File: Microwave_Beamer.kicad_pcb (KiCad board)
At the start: 6 copper layers, 200 x 170 mm, 408 parts, among them IC1 MAX2870ETJ+, U1 SKY13575-639LF, U10 SKY13575-639LF, U11 SKY13575-639LF, U12 SKY13575-639LF, U13 SE5023L-R, U14 SE5023L-R, U15 SE5023L-R, U16 SE5023L-R, U17 SE5023L-R, U18 SE5023L-R, U19 SE5023L-R, U2 SKY13575-639LF, U20 SE5023L-R, U21 SE5023L-R, U22 SE5023L-R, U23 SE5023L-R, U24 SE5023L-R, U25 SE5023L-R, U26 SE5023L-R, U27 SE5023L-R, U28 SE5023L-R, U29 SE5023L-R, U3 SKY13575-639LF, U30 SE5023L-R, U31 SE5023L-R, U32 SE5023L-R, U33 SE5023L-R, U34 SE5023L-R, U35 SE5023L-R, U36 SE5023L-R, U37 SE5023L-R, U38 SE5023L-R, U39 SE5023L-R, U4 SKY13575-639LF, U40 SE5023L-R, U41 SE5023L-R, U42 SE5023L-R, U43 SE5023L-R, U44 SE5023L-R, U45 SE5023L-R, U46 SE5023L-R, U47 SE5023L-R, U48 SE5023L-R, U49 SE5023L-R, U5 SKY13575-639LF, U50 LDL1117S33R, U51 SN74LVC1G14DCKR, U52 MIC5219-2.85YM5-TR, U53 SN74LVC1G14DCKR, U54 74HC138D, U55 TPS548D26RXXR, U56 PI_PICO, U57 SN74LVC1G14DCKR, U6 SKY13575-639LF, U7 SKY13575-639LF, U8 SKY13575-639LF, U9 SKY13575-639LF, Y1 ECS-3225MVQ-1000-CN-TR

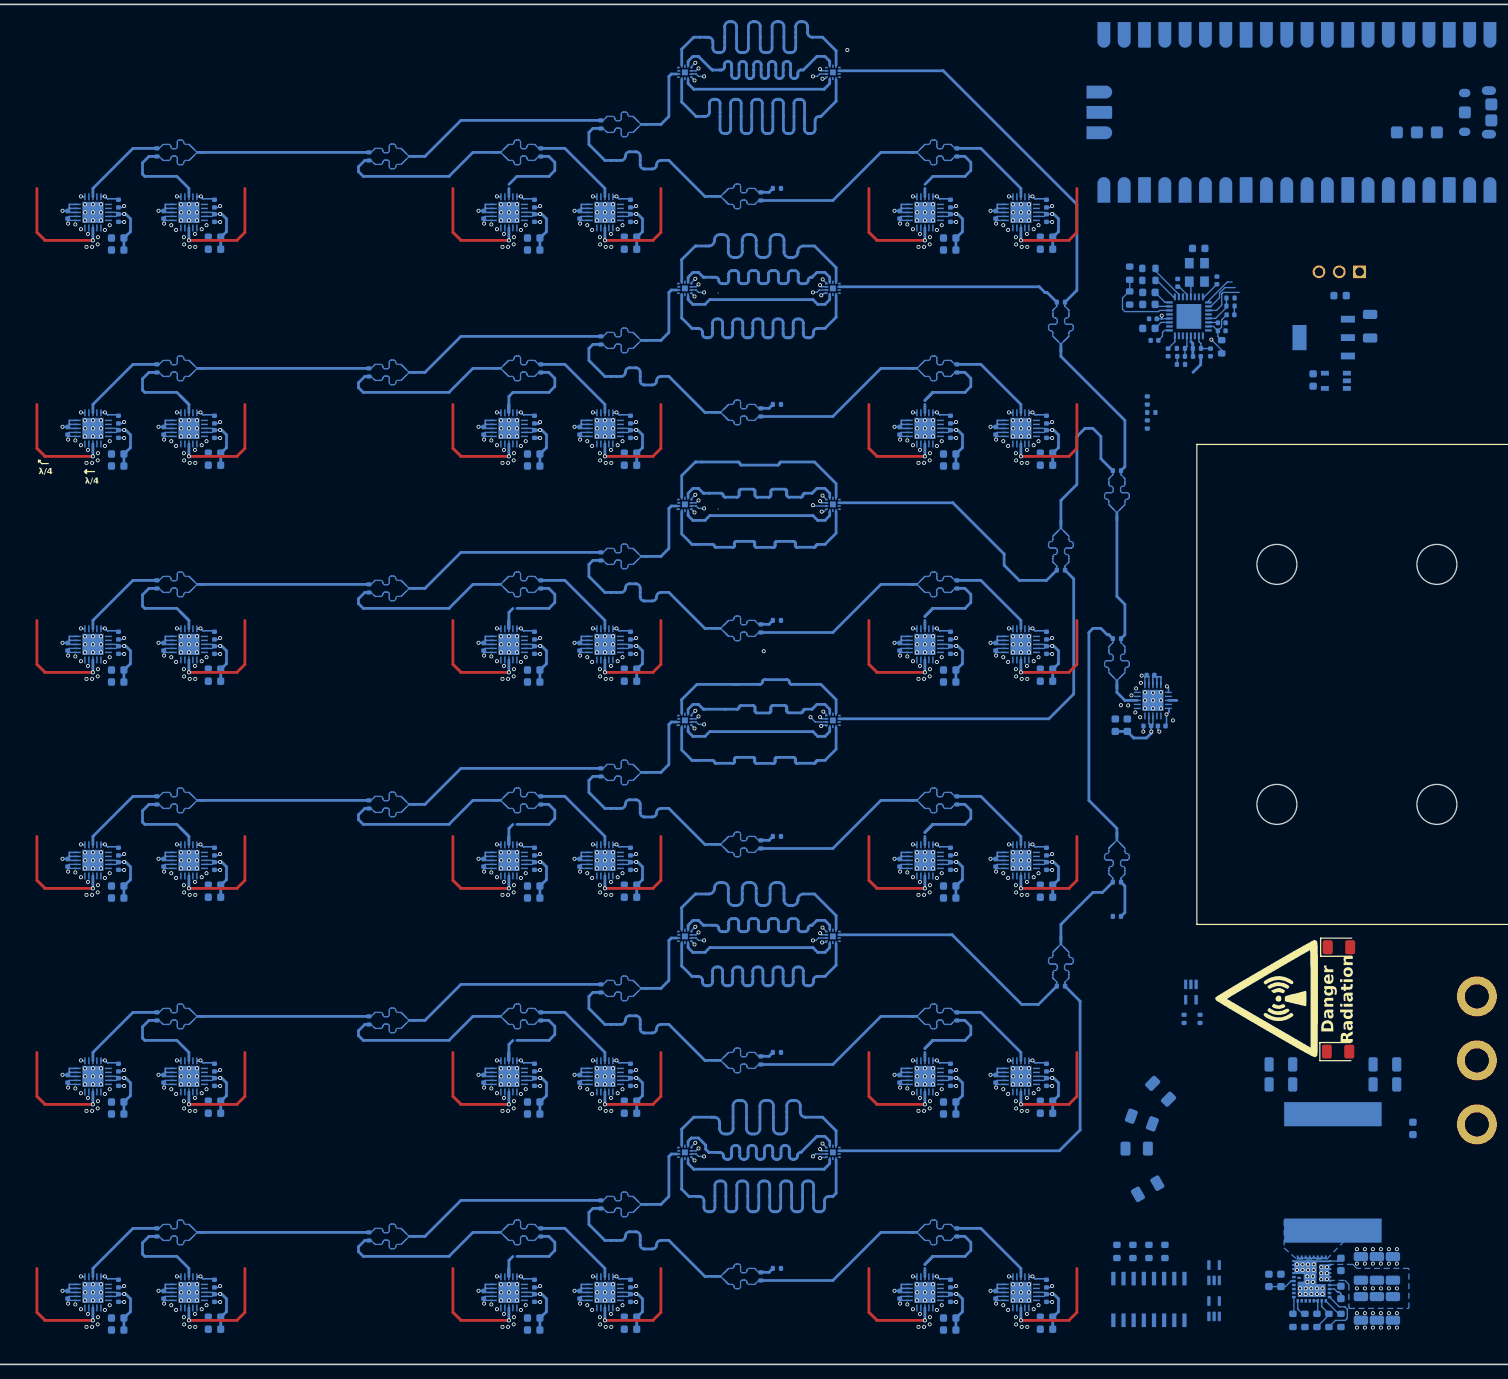
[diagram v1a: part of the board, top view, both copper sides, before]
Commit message: completed length matching
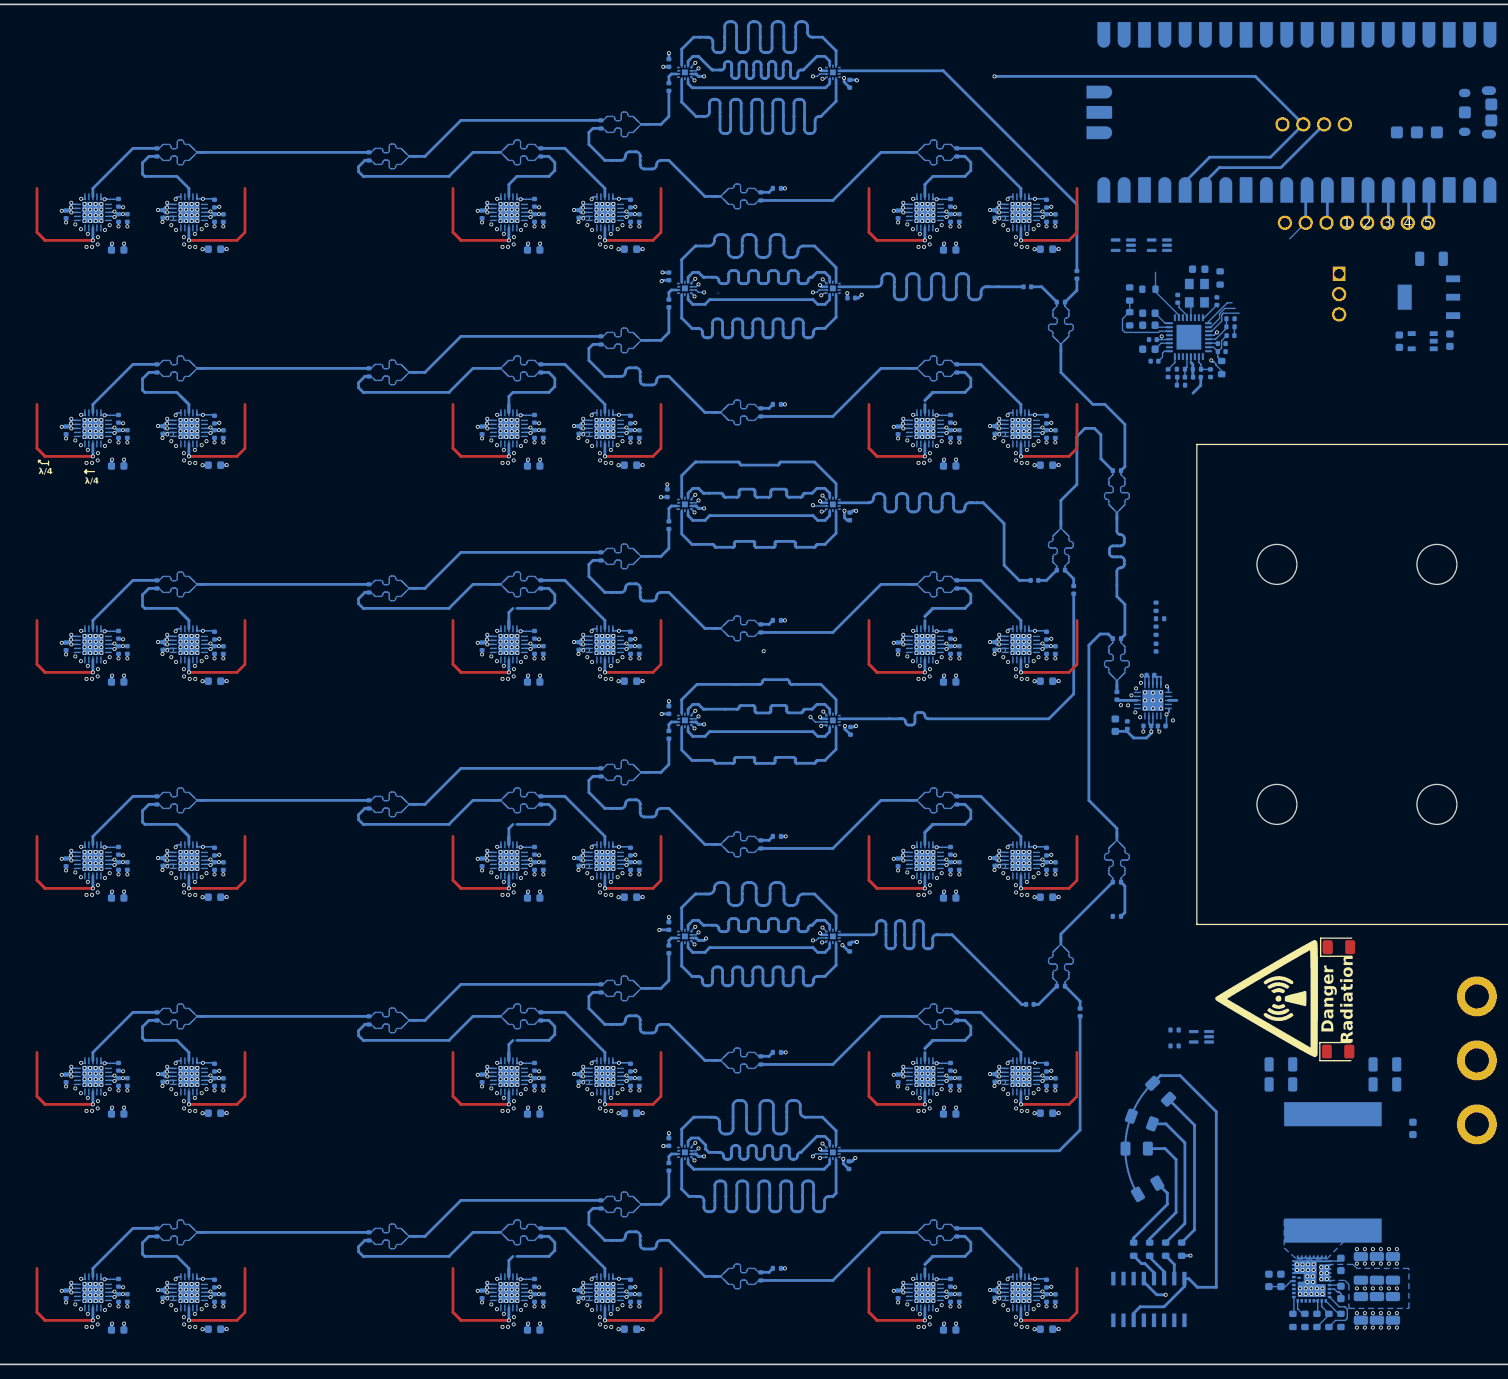
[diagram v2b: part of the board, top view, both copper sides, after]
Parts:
- added 1: , , F.Cu at (188.7, 32.3)
- added 2: , , F.Cu at (191.3, 32.3)
- added 3: , , F.Cu at (193.8, 32.3)
- added 4: , , F.Cu at (196.4, 32.3)
- added 5: , , F.Cu at (198.9, 32.3)
- added ?: , , F.Cu at (185.9, 20.0)
- added ?: , , F.Cu at (188.5, 20.0)
- added ?: , , F.Cu at (183.3, 20.0)
- added ?: , , F.Cu at (186.2, 32.3)
- added ?: , , F.Cu at (183.6, 32.3)
- added ?: , , F.Cu at (180.7, 20.0)
- added ?: , , F.Cu at (181.0, 32.3)
- added C139: 2.2pF, Capacitor_SMD:C_0402_1005Metric, B.Cu at (160.0, 91.4)
- added C140: 10nF, Capacitor_SMD:C_0402_1005Metric, B.Cu at (126.6, 14.9)
- added C147: 10nF, Capacitor_SMD:C_0402_1005Metric, B.Cu at (126.8, 41.7)
- added C148: 10nF, Capacitor_SMD:C_0402_1005Metric, B.Cu at (103.8, 66.1)
- added C149: 10nF, Capacitor_SMD:C_0402_1005Metric, B.Cu at (104.0, 93.2)
- added C151: 10nF, Capacitor_SMD:C_0402_1005Metric, B.Cu at (104.0, 120.2)
- added C152: 10nF, Capacitor_SMD:C_0402_1005Metric, B.Cu at (126.5, 150.1)
- added C153: 10nF, Capacitor_SMD:C_0402_1005Metric, B.Cu at (104.0, 12.3)
- added C154: 10nF, Capacitor_SMD:C_0402_1005Metric, B.Cu at (104.0, 147.2)
- added C155: 10nF, Capacitor_SMD:C_0402_1005Metric, B.Cu at (104.0, 39.0)
- added C156: 10nF, Capacitor_SMD:C_0402_1005Metric, B.Cu at (126.6, 69.0)
- added C158: 10nF, Capacitor_SMD:C_0402_1005Metric, B.Cu at (126.7, 95.8)
- added C160: 10nF, Capacitor_SMD:C_0402_1005Metric, B.Cu at (126.6, 122.9)
- added C161: 2.2pF, Capacitor_SMD:C_0402_1005Metric, B.Cu at (104.0, 15.3)
- added C162: 2.2pF, Capacitor_SMD:C_0402_1005Metric, B.Cu at (104.0, 42.4)
- added C163: 2.2pF, Capacitor_SMD:C_0402_1005Metric, B.Cu at (104.0, 70.1)
- added C165: 2.2pF, Capacitor_SMD:C_0402_1005Metric, B.Cu at (104.0, 96.3)
- added C166: 2.2pF, Capacitor_SMD:C_0402_1005Metric, B.Cu at (104.0, 123.1)
- added C167: 2.2pF, Capacitor_SMD:C_0402_1005Metric, B.Cu at (104.0, 150.3)
- added C168: 2.2pF, Capacitor_SMD:C_0402_1005Metric, B.Cu at (155.0, 38.8)
- added C169: 2.2pF, Capacitor_SMD:C_0402_1005Metric, B.Cu at (148.8, 40.3)
- added C170: 2.2pF, Capacitor_SMD:C_0402_1005Metric, B.Cu at (149.7, 77.0)
- added C172: 2.2pF, Capacitor_SMD:C_0402_1005Metric, B.Cu at (154.6, 78.2)
- added C174: 2.2pF, Capacitor_SMD:C_0402_1005Metric, B.Cu at (149.1, 130.0)
- added C175: 2.2pF, Capacitor_SMD:C_0402_1005Metric, B.Cu at (155.4, 131.0)
- added C176: 2.2pF, Capacitor_SMD:C_0402_1005Metric, B.Cu at (164.9, 85.4)
- C107, C111, C114, C119, C12, C14, C16, C19, C21, C23, C25, C27, C28, C29, C30, C33, C35, C37, C39, C4, C41, C42, C43, C44, C46, C48, C49, C50, C6, C7, C71, C8, C82, C85, C9, C96, C99: footprint Capacitor_SMD:C_0603_1608Metric -> Capacitor_SMD:C_0402_1005Metric
- C285, C286, C287, C288, C289, C290, C291, C292, C293, C294, C295, C296, C297, C298, C299, C300, C301, C302, C303, C304, C305, C306, C307, C308, C309, C310, C311, C312, C313, C314, C315, C316, C317, C318, C319, C320, C321: value 10nF -> 100nF
- moved U53 133.1 mm to (165.3, 35.1), turned to 180 degrees
- moved U51 128.9 mm to (160.8, 35.1), turned to 180 degrees
- moved RR4 25.8 mm to (164.9, 80.3)
- moved RR5 25.8 mm to (165.4, 81.8)
- moved RR6 25.8 mm to (164.9, 83.3)
- moved C283 14.8 mm to (201.6, 47.0), turned to -90 degrees
- moved U50 14.1 mm to (199.0, 41.6)
- moved U52 11.9 mm to (198.2, 47.1)
- moved C284 11.8 mm to (195.3, 47.1)
- moved CB13 11.4 mm to (199.3, 36.8), turned to 0 degrees
- moved R54 8.91 mm to (172.9, 39.2), turned to 90 degrees
- moved U57 5.74 mm to (170.6, 134.1), turned to 180 degrees
- moved PS1 4.90 mm to (186.0, 41.2), turned to -90 degrees
- moved R61 4.64 mm to (167.2, 135.2), turned to 180 degrees
- moved C7 2.77 mm to (140.3, 31.7), turned to -90 degrees
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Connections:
- R4 pad 1: Net-(U1-RFC) -> Net-(W4-Out1)
- R4 pad 2: Net-(U2-RFC) -> Net-(W4-Out2)
- R5 pad 1: Net-(U3-RFC) -> Net-(W5-Out1)
- R5 pad 2: Net-(U4-RFC) -> Net-(W5-Out2)
- R6 pad 1: Net-(U5-RFC) -> Net-(W6-Out1)
- R6 pad 2: Net-(U6-RFC) -> Net-(W6-Out2)
- RR6 pad 2: /POWER AMP6/RF_IN -> Net-(C176-Pad1)
- U10 pad 2: /STEM/FAN_D/IN -> Net-(U10-RFC)
- U11 pad 2: /STEM/FAN_E/IN -> Net-(U11-RFC)
- U12 pad 2: /STEM/FAN_F/IN -> Net-(U12-RFC)
- U7 pad 2: /STEM/FAN_A/IN -> Net-(U7-RFC)
- U8 pad 2: /STEM/FAN_B/IN -> Net-(U8-RFC)
- U9 pad 2: /STEM/FAN_C/IN -> Net-(U9-RFC)
- W1 pad 1: /POWER AMP6/RF_OUT -> /STEM/IN
- W4 pad 2: Net-(U1-RFC) -> Net-(W4-Out1)
- W4 pad 3: Net-(U2-RFC) -> Net-(W4-Out2)
- W5 pad 2: Net-(U3-RFC) -> Net-(W5-Out1)
- W5 pad 3: Net-(U4-RFC) -> Net-(W5-Out2)
- W6 pad 2: Net-(U5-RFC) -> Net-(W6-Out1)
- W6 pad 3: Net-(U6-RFC) -> Net-(W6-Out2)
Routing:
- net +5V: track 521.6 -> 410.3 mm, vias 73 -> 289
- net PHASE_CTRL_1: track 146.5 -> 225.4 mm, vias 6 -> 7
- net +3.3V: track 301.7 -> 379.6 mm, vias 13 -> 24
- net 5V_LP: track 3.41 -> 49.6 mm
- net Net-(D4-K): track 0.00 -> 19.9 mm
- net 2.85VREF: track 952.1 -> 972.0 mm
- net Net-(D1-K): track 0.00 -> 18.5 mm
- net PHASE_CTRL_2: track 150.7 -> 168.1 mm
- net Net-(D2-K): track 0.00 -> 15.8 mm
- net GND: track 188.7 -> 175.2 mm, vias 833 -> 1193
- net /led_n45: track 0.00 -> 12.3 mm, vias 0 -> 2
- net Net-(U2-RFC): track 33.6 -> 43.9 mm
- net Net-(U6-RFC): track 55.6 -> 45.4 mm
- net Net-(U1-RFC): track 55.1 -> 45.0 mm
- net Net-(D3-K): track 0.00 -> 9.69 mm
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- added copper zone on In3.Cu, net +5V
